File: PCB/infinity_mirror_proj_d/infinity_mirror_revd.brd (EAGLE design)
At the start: 160 x 100 mm, 17 parts, among them J1 5.5x2.1mm Barrel, Q1 800mA/40V, Q2 800mA/40V, U1 3.3LDO

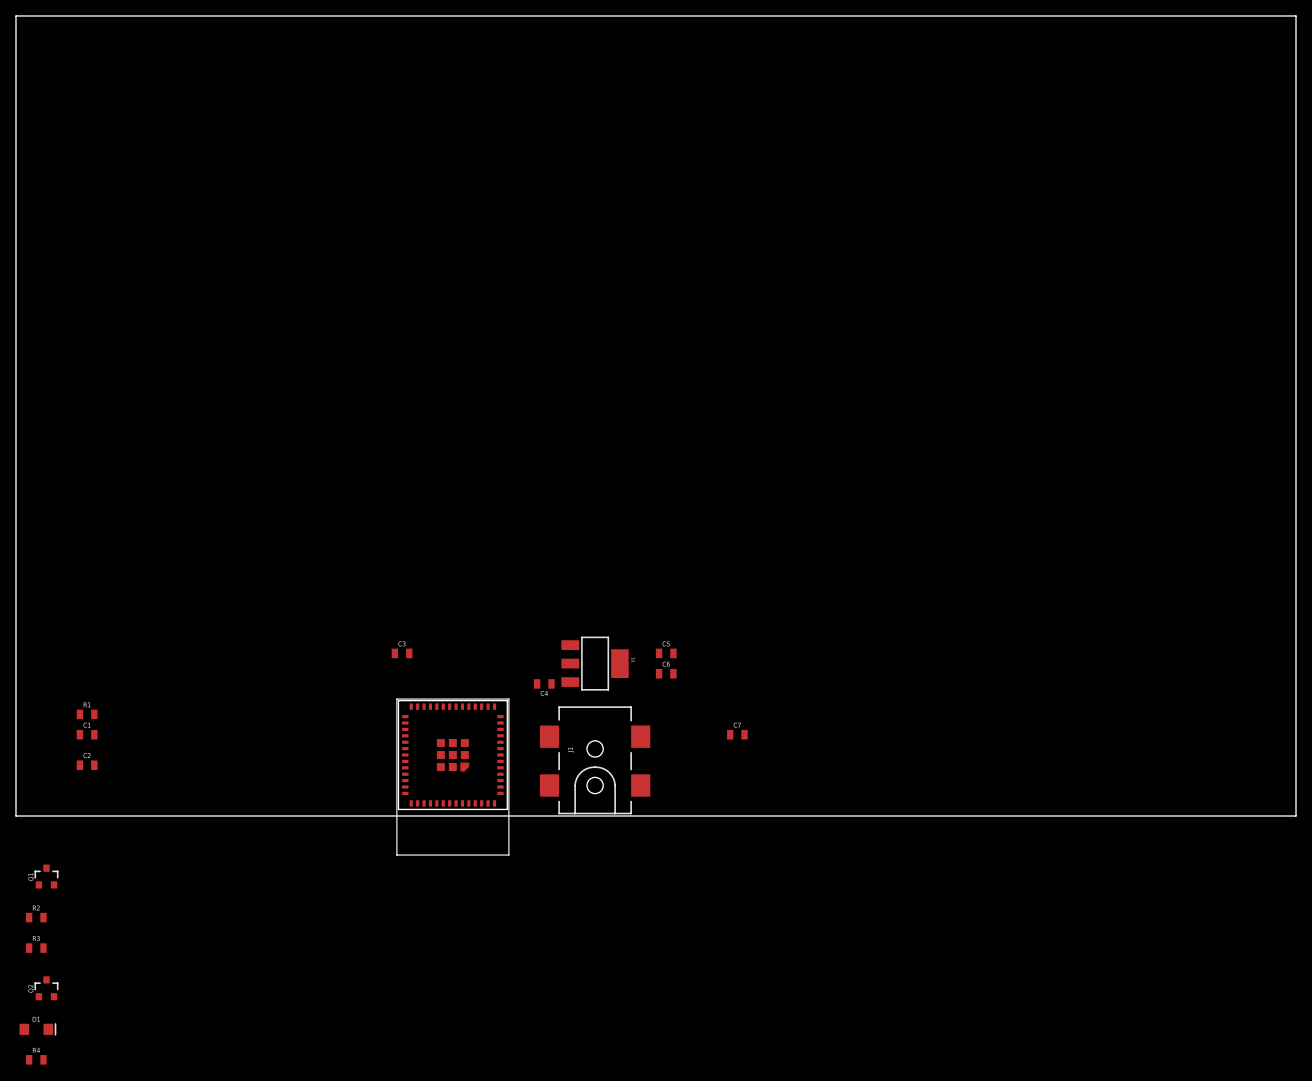
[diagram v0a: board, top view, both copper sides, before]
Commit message: 1st draft schematic and board complete, needs review
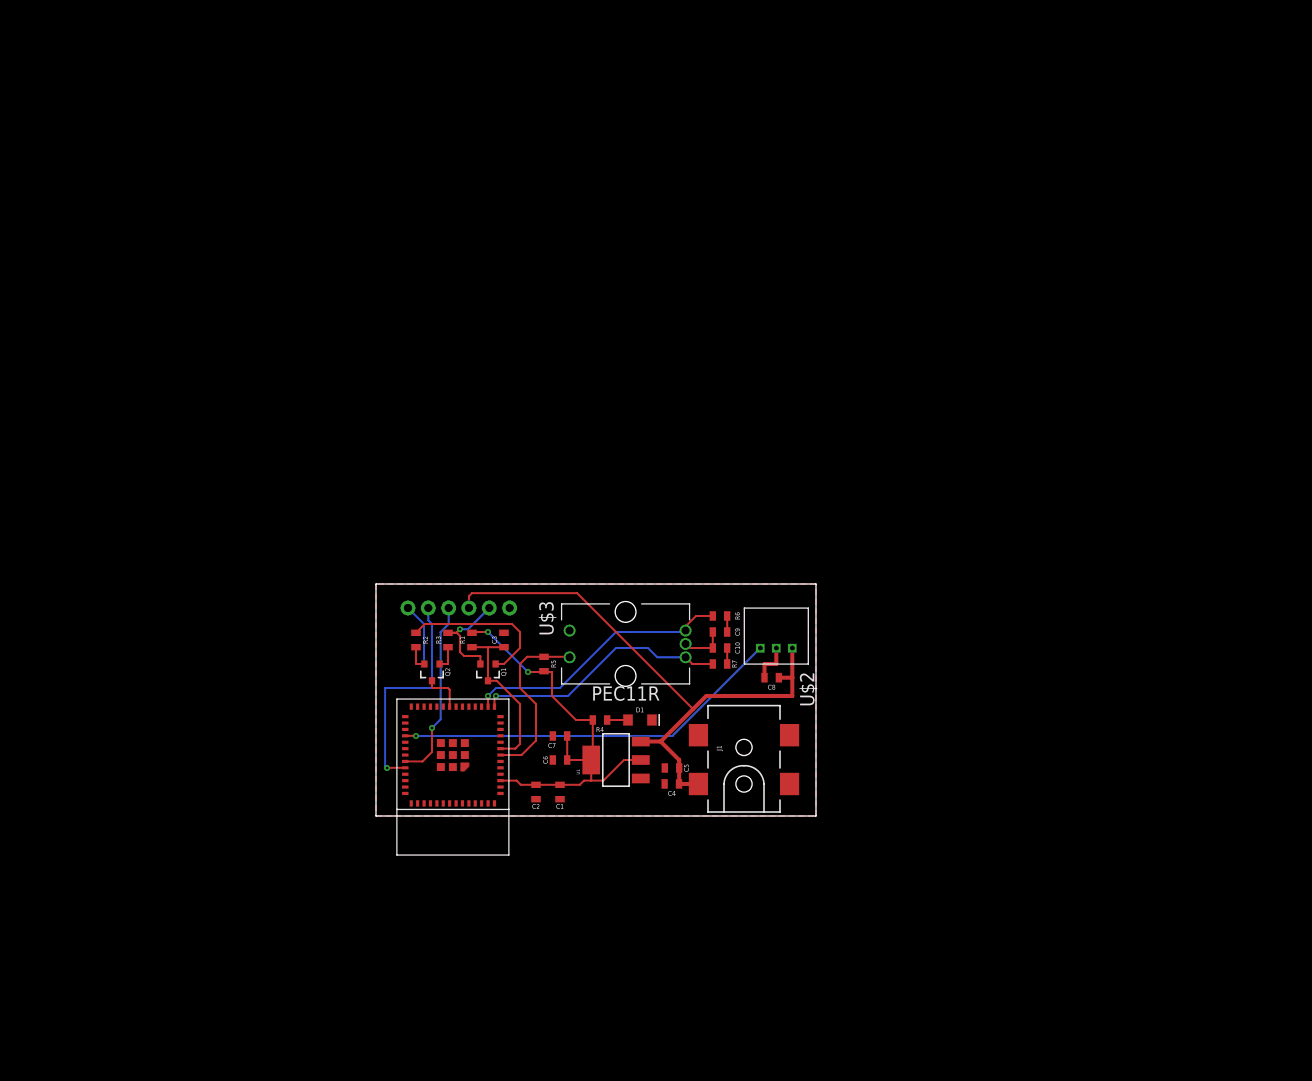
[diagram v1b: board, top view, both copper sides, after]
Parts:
- added C10, C9: 0.1uF, _111_IH:0805
- added C8: 1000uF, _111_IH:0805
- added J2: (no value), SparkFun-Connectors:1X06
- added R5, R6, R7: 10k, _111_IH:0805
- added U$2: 3-PIN-JST, infinity_mirror_revd:3-PIN-JST
- added U$3: PEC11R, infinity_mirror_revd:PEC11R-4320F-S0012
- R4: value 10k -> 5.1K
- moved D1 84.8 mm to (78.0, 12.0)
- moved R4 82.3 mm to (73.0, 12.0), turned to 180 degrees
- moved R3 64.3 mm to (54.0, 22.0), turned to 90 degrees
- moved Q2 62.4 mm to (52.0, 18.0), turned to 180 degrees
- moved Q1 60.8 mm to (59.0, 18.0), turned to 180 degrees
- moved C1 59.5 mm to (68.0, 3.00), turned to 270 degrees
- moved R2 58.8 mm to (50.0, 22.0), turned to 270 degrees
- moved C2 56.2 mm to (65.0, 3.00), turned to 270 degrees
- moved R1 49.0 mm to (57.0, 22.0), turned to 90 degrees
- moved C7 22.2 mm to (68.0, 10.0), turned to 180 degrees
- moved C4 20.3 mm to (82.0, 4.01)
- moved J1 18.6 mm to (91.0, 4.00)
- moved C6 17.1 mm to (68.0, 7.00), turned to 180 degrees
- moved C5 14.3 mm to (82.0, 6.00), turned to 180 degrees
- moved C3 12.9 mm to (61.0, 22.0), turned to 90 degrees
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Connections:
- net N$1 renamed Q1_BASE
- net N$2 renamed LED+
- net N$3 renamed Q2_BASE
- removed net GPIO23: U$1.31
- removed net N$22: U$1.34
- removed net N$35: U$1.15
- removed net N$36: U$1.14
- removed net N$7: U$1.7
- new net BUTTON: R5.1, U$1.7, U$3.VCC
- new net ENCODER_A: R7.1, U$1.14, U$3.A
- new net ENCODER_B: R6.2, U$1.15, U$3.B
- new net LED_DATA: U$1.31, U$2.P$3
- new net N$15: C10.1, R7.2
- new net N$19: C9.1, R6.1
- net DTR: now also J2.1
- net GND: now also C10.2, C8.2, C9.2, J2.6, U$2.P$2, U$3.C, U$3.GND
- net RTS: now also J2.5
- net U0RXD: now also J2.3
- net U0TXD: now also J2.2
- net VCC_1: now also C8.1, J2.4, U$2.P$1
- net VCC_2: now also R5.2
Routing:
- net VCC_1: track 0.00 -> 73.3 mm
- net VCC_2: track 0.00 -> 54.4 mm, vias 0 -> 2
- net LED_DATA: track 0.00 -> 48.9 mm, vias 0 -> 1
- net ENCODER_B: track 0.00 -> 33.9 mm, vias 0 -> 1
- net ENCODER_A: track 0.00 -> 31.8 mm, vias 0 -> 1
- net U0TXD: track 0.00 -> 28.4 mm, vias 0 -> 1
- net U0RXD: track 0.00 -> 22.7 mm, vias 0 -> 1
- net BUTTON: track 0.00 -> 22.2 mm
- net ESP_RST: track 0.00 -> 21.1 mm
- net Q1_BASE: track 0.00 -> 19.7 mm
- net RTS: track 0.00 -> 13.8 mm, vias 0 -> 1
- net DTR: track 0.00 -> 10.9 mm
- net GND: track 0.00 -> 10.8 mm
- net GPIO0: track 0.00 -> 5.32 mm
- net Q2_BASE: track 0.00 -> 3.15 mm
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- added copper zone on layer 1, net GND
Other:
- board size 160 x 100 mm -> 55 x 29 mm

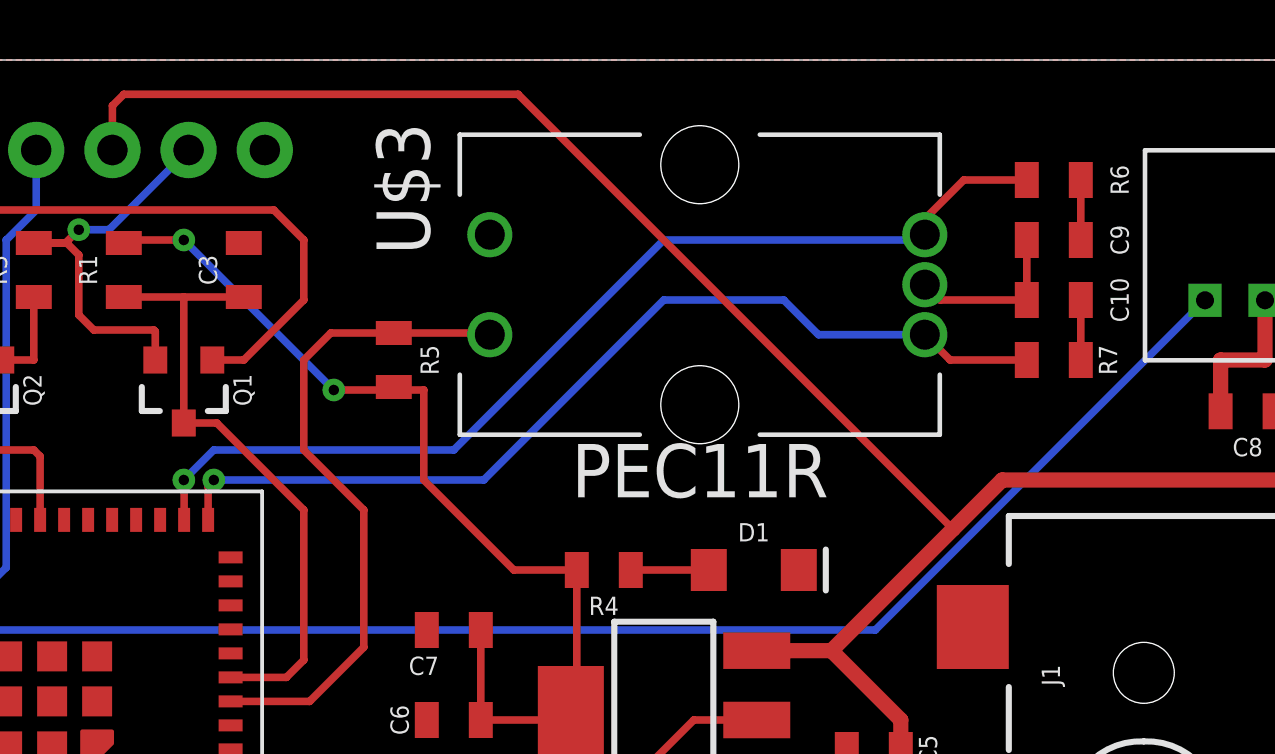
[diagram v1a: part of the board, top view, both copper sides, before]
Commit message: fixed encoder schematic
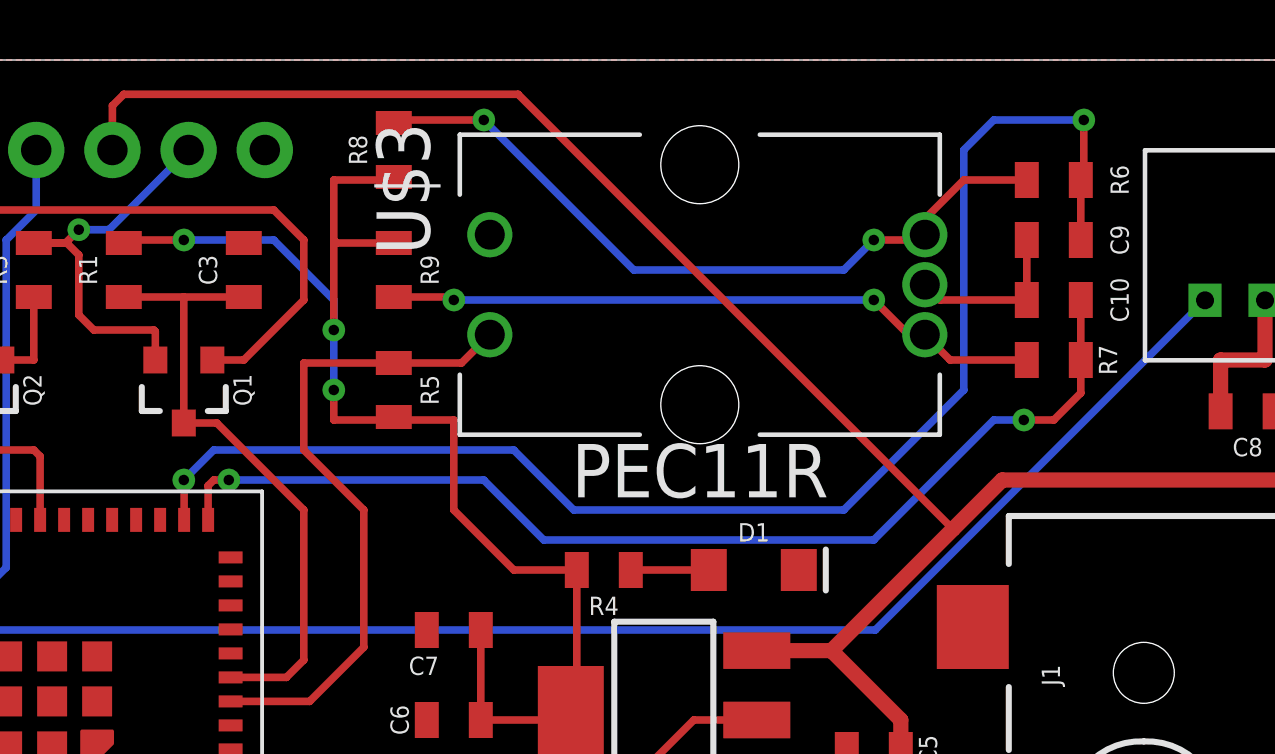
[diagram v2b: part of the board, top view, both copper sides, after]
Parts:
- added R8, R9: 10k, _111_IH:0805
- moved R5 1.00 mm to (66.0, 18.0)
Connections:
- removed net ENCODER_A: R7.1, U$1.14, U$3.A
- removed net ENCODER_B: R6.2, U$1.15, U$3.B
- removed net N$15: C10.1, R7.2
- removed net N$19: C9.1, R6.1
- new net ENC_A: C10.1, R7.2, U$1.14
- new net ENC_B: C9.1, R6.1, U$1.15
- new net N$2: R6.2, R8.2, U$3.B
- new net N$3: R7.1, R9.2, U$3.A
- net VCC_2: now also R8.1, R9.1
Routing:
- net ENC_B: track 0.00 -> 46.7 mm, vias 0 -> 2
- net ENC_A: track 0.00 -> 36.3 mm, vias 0 -> 2
- net ENCODER_B: track 33.9 -> 0.00 mm, vias 1 -> 0
- net ENCODER_A: track 31.8 -> 0.00 mm, vias 1 -> 0
- net N$2: track 0.00 -> 24.8 mm, vias 0 -> 2
- net N$3: track 0.00 -> 22.0 mm, vias 0 -> 2
- net VCC_2: track 54.4 -> 65.5 mm, vias 2 -> 3
- net N$19: track 2.00 -> 0.00 mm
- net N$15: track 2.00 -> 0.00 mm

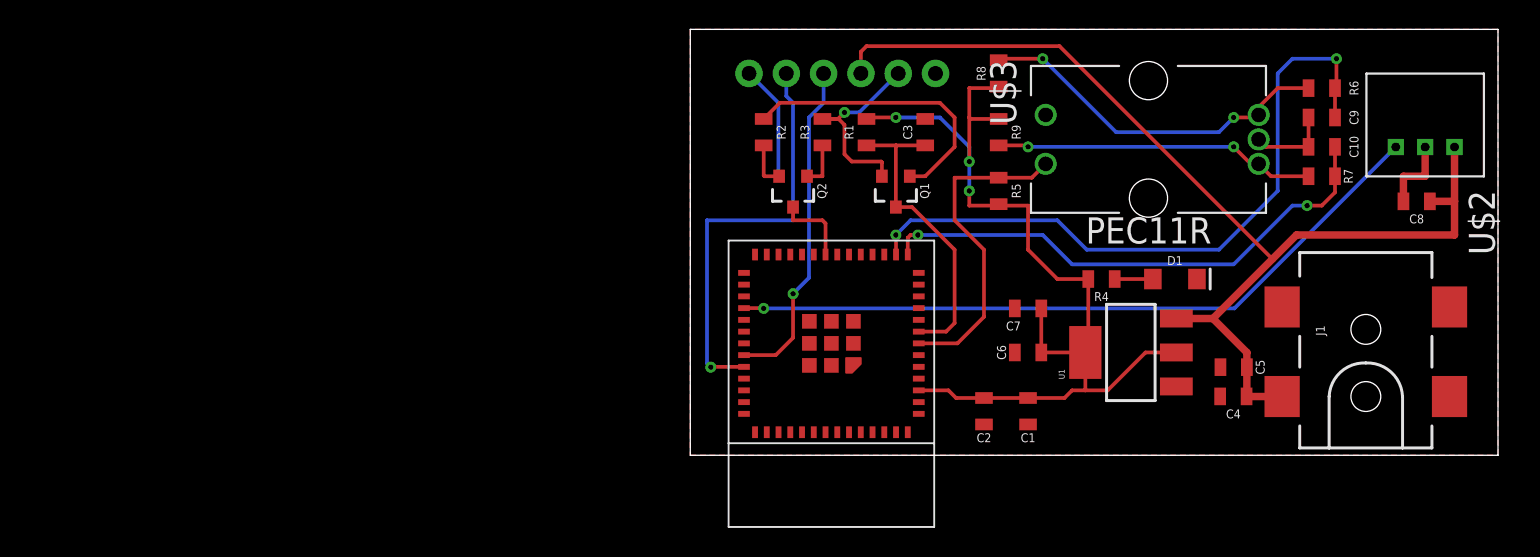
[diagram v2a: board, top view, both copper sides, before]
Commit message: added logic level shifting for LEDs and buttons for programming
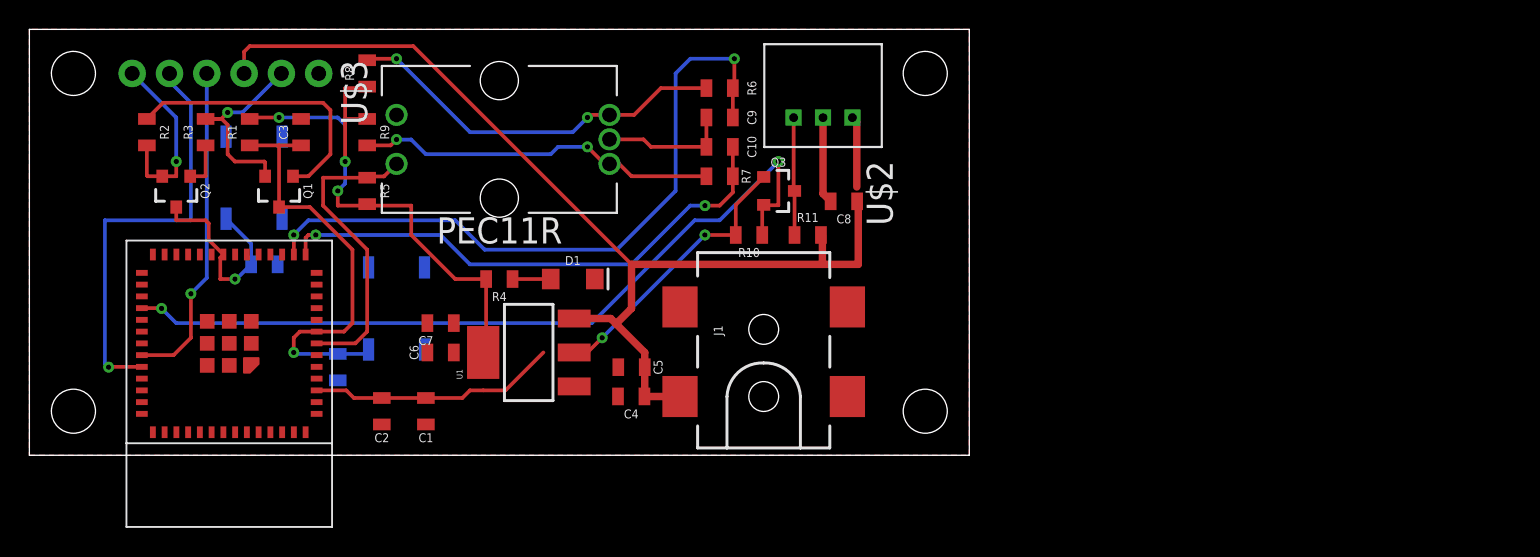
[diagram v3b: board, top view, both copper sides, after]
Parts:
- added C11, C12: 0.1uF, _111_IH:0805
- added Q3: BSS138, SparkFun-DiscreteSemi:SOT23-3
- added R10, R11: 10k, _111_IH:0805
- added S1, S2: SWITCH, SparkFun-Switches:TACTILE_SWITCH_SMD_5.2MM
- J2: value (none) -> HEADER
- moved U$3 44.2 mm to (32.0, 21.5)
- moved R5 43.0 mm to (23.0, 18.0)
- moved R8 43.0 mm to (23.0, 26.0)
- moved R9 43.0 mm to (23.0, 22.0)
- moved C3 42.5 mm to (18.5, 22.0)
- moved J2 42.0 mm to (7.00, 26.0)
- moved Q1 42.0 mm to (17.0, 18.0)
- moved Q2 42.0 mm to (10.0, 18.0)
- moved R1 42.0 mm to (15.0, 22.0)
- moved R2 42.0 mm to (8.00, 22.0)
- moved R3 42.0 mm to (12.0, 22.0)
- moved U$2 41.0 mm to (54.0, 23.0)
- moved C4 41.0 mm to (41.0, 4.01)
- moved C1 41.0 mm to (27.0, 3.00)
- moved C10 41.0 mm to (47.0, 21.0)
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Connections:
- removed net N$1: U$1.10
- removed net N$11: U$1.11
- removed net N$12: U$1.12
- removed net N$13: U$1.13
- removed net N$17: U$1.29
- removed net N$18: U$1.30
- removed net N$20: U$1.32
- removed net N$21: U$1.33
- removed net N$24: U$1.26
- removed net N$25: U$1.25
- removed net N$28: U$1.22
- removed net N$30: U$1.20
- removed net N$31: U$1.19
- removed net N$32: U$1.18
- removed net N$33: U$1.17
- removed net N$34: U$1.16
- removed net N$5: U$1.5
- removed net N$6: U$1.6
- removed net N$9: U$1.9
- new net IO23: Q3.2, R10.1, U$1.31
- net ESP_RST: now also C12.2, S2.3
- net GND: now also C11.1, C12.1, S1.1, S2.1
- net GPIO0: now also C11.2, S1.3
- net LED_DATA: now also Q3.3, R11.1; no longer U$1.31
- net VCC_1: now also R11.2
- net VCC_2: now also Q3.1, R10.2
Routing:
- net IO23: track 0.00 -> 54.4 mm, vias 0 -> 2
- net LED_DATA: track 48.9 -> 8.01 mm, vias 1 -> 0
- net ESP_RST: track 21.1 -> 29.7 mm, vias 0 -> 1
- net VCC_2: track 65.5 -> 74.1 mm, vias 3 -> 5
- net GPIO0: track 5.32 -> 13.8 mm, vias 0 -> 1
- net GND: track 10.8 -> 14.7 mm
- net VCC_1: track 73.3 -> 76.4 mm
- net N$3: track 22.0 -> 24.7 mm
- net N$2: track 24.8 -> 26.5 mm
- net DTR: track 10.9 -> 12.3 mm, vias 0 -> 1
- net BUTTON: track 22.1 -> 20.9 mm
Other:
- board size 55 x 29 mm -> 64 x 29 mm
